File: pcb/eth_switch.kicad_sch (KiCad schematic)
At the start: 9 parts, among them IC1 IP175G, J1 100616-2

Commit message: More schematic
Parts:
- added C23: 100n, Capacitor_SMD:C_0603_1608Metric_Pad1.08x0.95mm_HandSolder, symbol Device:C
- added D3, D4, D5, D6, D7, D8: ~, LED_SMD:LED_0603_1608Metric_Pad1.05x0.95mm_HandSolder, symbol Device:LED
- added J3: Conn_01x04, Connector_PinHeader_1.00mm:PinHeader_1x04_P1.00mm_Vertical, symbol Connector_Generic:Conn_01x04
- added JP1: SolderJumper_3_Bridged12, Jumper:SolderJumper-3_P1.3mm_Bridged12_Pad1.0x1.5mm, symbol Jumper:SolderJumper_3_Bridged12
- added R19, R20: 10k, Resistor_SMD:R_0603_1608Metric_Pad0.98x0.95mm_HandSolder, symbol Device:R
- added R21, R22, R23, R24, R25, R26, R27, R28, R29, R30, R31, R32, R33, R34, R35, R36, R37, R38, R39, R40: 2R2, Resistor_SMD:R_0603_1608Metric, symbol Device:R
- added R41, R42, R43, R44, R45, R46: 330, Resistor_SMD:R_0603_1608Metric_Pad0.98x0.95mm_HandSolder, symbol Device:R
- added U5: 24LC02, Package_SO:SOIC-8_3.9x4.9mm_P1.27mm, symbol Memory_EEPROM:24LC02
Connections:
- net 1TX1_N: now reaches IC1.1 (TXOM1)
- net 1TX1_N: now also R21.2
- net 2TX2_P: now reaches IC1.10 (TXOP2)
- net 2TX2_P: now also R26.2
- net 2TX2_N: now reaches IC1.11 (TXOM2)
- net 2TX2_N: now also R25.2
- net 3RX3_P: now reaches IC1.14 (RXIP3)
- net 3RX3_P: now also R33.2
- net 3RX3_N: now reaches IC1.15 (RXIM3)
- net 3RX3_N: now also R34.2
- net 3TX3_P: now reaches IC1.16 (TXOP3)
- net 3TX3_P: now also R35.2
- net 3TX3_N: now reaches IC1.17 (TXOM3)
- net 3TX3_N: now also R36.2
- net 4TX4_N: now reaches IC1.19 (TXOM4)
- net 4TX4_N: now also R37.2
- net 1TX1_P: now reaches IC1.2 (TXOP1)
- net 1TX1_P: now also R22.2
- net 4TX4_P: now reaches IC1.20 (TXOP4)
- net 4TX4_P: now also R38.2
- net 4RX4_N: now reaches IC1.21 (RXIM4)
- net 4RX4_N: now also R39.2
- net 4RX4_P: now reaches IC1.22 (RXIP4)
- net 4RX4_P: now also R40.2
- net 1RX1_N: now reaches IC1.3 (RXIM1)
- net 1RX1_N: now also R23.2
- net PWR_OFF: now reaches IC1.31 (F_POWER_OFF_LED_/_VLAN_DIS)
- net PWR_OFF: now also R46.1
- net LINK4: now reaches IC1.32 (LINK_LED4)
- net LINK4: now also R45.1
- net LINK3: now reaches IC1.33 (LINK_LED3)
- net LINK3: now also R44.1
- net LINK2: now reaches IC1.35 (LINK_LED2/RSVD_GMAC_FILTER)
- net LINK2: now also R43.1
- net LINK1: now reaches IC1.36 (LINK_LED1/SCLK/BF_STM_DIS)
- net LINK1: now also R42.1
- net LINK0: now reaches IC1.37 (LINK_LED0/SDATA/COS_DIS)
- net LINK0: now also R41.1
- net I2C_SCL: now reaches IC1.38 (SCL/MDC)
- net I2C_SCL: now also J3.3 (Pin_3), R19.1, U5.6 (SCL)
- net I2C_SDA: now reaches IC1.39 (SDA/MDIO)
- net I2C_SDA: now also J3.2 (Pin_2), R20.1, U5.5 (SDA)
- net 1RX1_P: now reaches IC1.4 (RXIP1)
- net 1RX1_P: now also R24.2
- net 0RX0_P: now reaches IC1.44 (RXIP0)
- net 0RX0_P: now also R32.2
- net 0RX0_N: now reaches IC1.45 (RXIM0)
- net 0RX0_N: now also R31.2
- net 0TX0_P: now reaches IC1.46 (TXOP0)
- net 0TX0_P: now also R30.2
- net 0TX0_N: now reaches IC1.47 (TXOM0)
- net 0TX0_N: now also R29.2
- net 2RX2_P: now reaches IC1.8 (RXIP2)
- net 2RX2_P: now also R28.2
- net 2RX2_N: now reaches IC1.9 (RXIM2)
- net 2RX2_N: now also R27.2
- new net: D7.1 (K), R45.2
- new net: D6.1 (K), R44.2
- new net: D5.1 (K), R43.2
- new net: D4.1 (K), R42.2
- new net: D3.1 (K), R41.2
- new net: D8.1 (K), R46.2
- new net: JP1.2 (C), U5.7 (WP)
- new net +3.3V: C23.1, D3.2 (A), D4.2 (A), D5.2 (A), D6.2 (A), D7.2 (A), D8.2 (A), J3.1 (Pin_1), JP1.1 (A), R19.2, R20.2, U5.8 (VCC)
- new net GND: C23.2, J3.4 (Pin_4), JP1.3 (B), U5.1 (A0), U5.2 (A1), U5.3 (A2), U5.4 (GND)
- new net RX0_N: R31.1
- new net RX0_P: R32.1
- new net RX1_N: R23.1
- new net RX1_P: R24.1
- new net RX2_N: R27.1
- new net RX2_P: R28.1
- new net RX3_N: R34.1
- new net RX3_P: R33.1
- new net RX4_N: R39.1
- new net RX4_P: R40.1
- new net TX0_N: R29.1
- new net TX0_P: R30.1
- new net TX1_N: R21.1
- new net TX1_P: R22.1
- new net TX2_N: R25.1
- new net TX2_P: R26.1
- new net TX3_N: R36.1
- new net TX3_P: R35.1
- new net TX4_N: R37.1
- new net TX4_P: R38.1

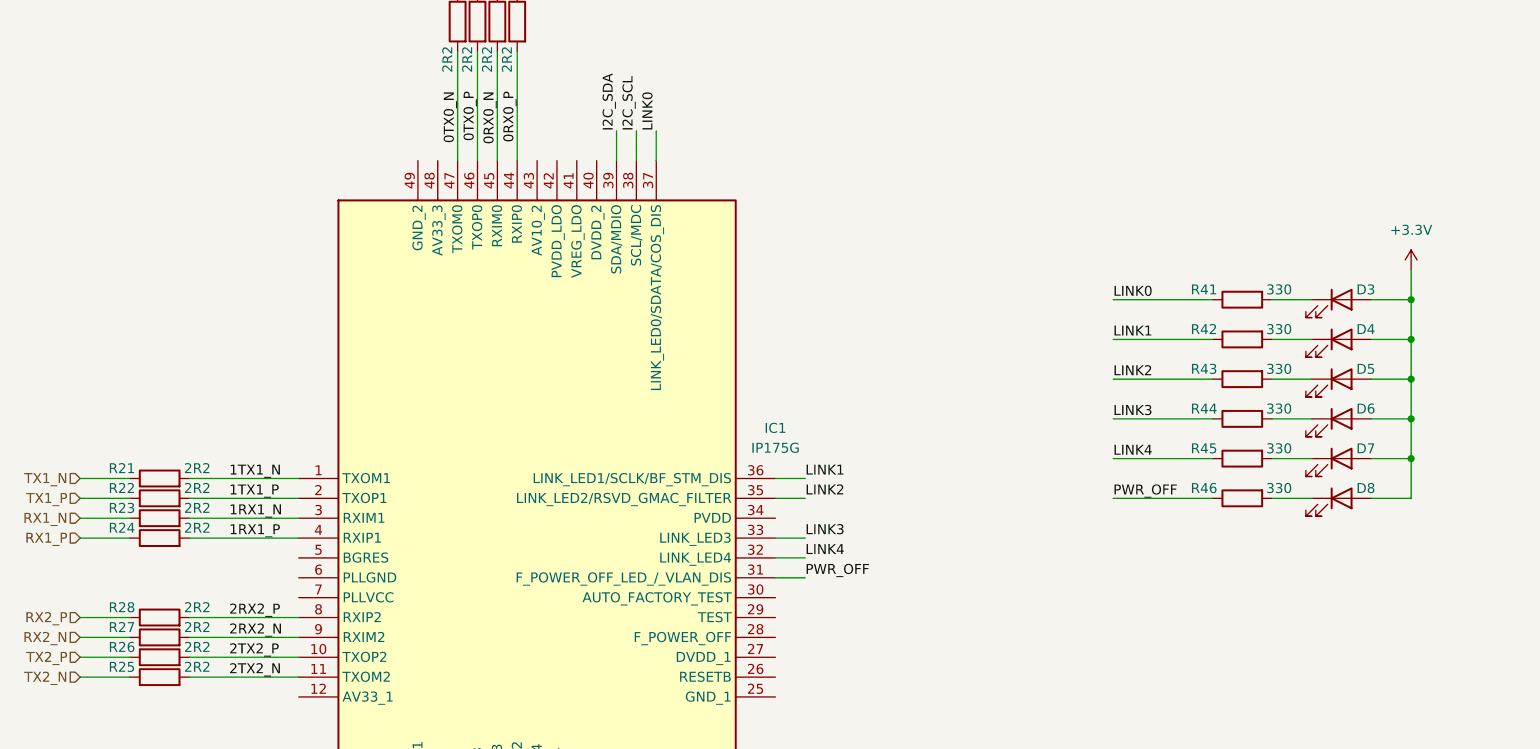
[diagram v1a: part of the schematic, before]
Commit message: Add symbols and adjust component positions in eth_switch schematic
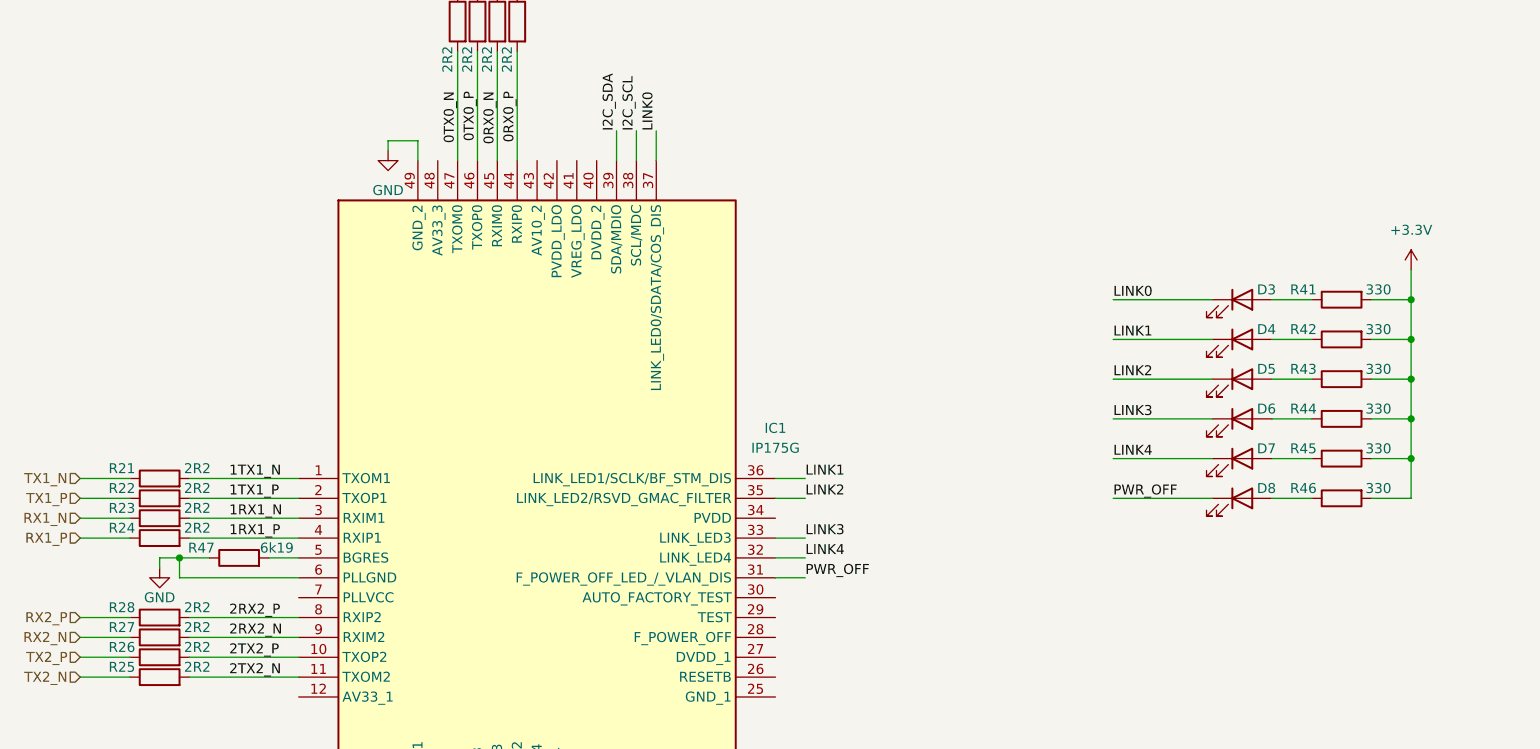
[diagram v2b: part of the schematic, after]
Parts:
- added R47: 6k19, Resistor_SMD:R_0603_1608Metric, symbol Device:R
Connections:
- net +3.3V: now also R41.2, R42.2, R43.2, R44.2, R45.2, R46.2; no longer D3.2 (A), D4.2 (A), D5.2 (A), D6.2 (A), D7.2 (A), D8.2 (A)
- net GND: now also IC1.49 (GND_2), IC1.6 (PLLGND), R47.1
- net LINK0: now also D3.1 (K); no longer R41.1
- net LINK1: now also D4.1 (K); no longer R42.1
- net LINK2: now also D5.1 (K); no longer R43.1
- net LINK3: now also D6.1 (K); no longer R44.1
- net LINK4: now also D7.1 (K); no longer R45.1
- net PWR_OFF: now also D8.1 (K); no longer R46.1
- net at IC1.5 (BGRES): now also R47.2
- new net: D7.2 (A), R45.1
- new net: D6.2 (A), R44.1
- new net: D5.2 (A), R43.1
- new net: D4.2 (A), R42.1
- new net: D3.2 (A), R41.1
- new net: D8.2 (A), R46.1
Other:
- moved on the sheet: D3, D4, D5, D6, D7, D8, R41, R42, R43, R44, R45, R46

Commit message: Sch complete, starting pcb
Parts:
- added C10, C11, C12, C13, C14, C18, C19, C22, C23, C24, C25, C26, C27, C30, C31, C32, C35, C36, C9: 100n, Capacitor_SMD:C_0603_1608Metric_Pad1.08x0.95mm_HandSolder, symbol Device:C
- added C16, C20, C28, C7: 1u, Capacitor_SMD:C_0603_1608Metric_Pad1.08x0.95mm_HandSolder, symbol Device:C
- added C17, C21, C29, C8: 10u, Capacitor_SMD:C_1206_3216Metric_Pad1.33x1.80mm_HandSolder, symbol Device:C
- added C34: 1n, Capacitor_SMD:C_0603_1608Metric_Pad1.08x0.95mm_HandSolder, symbol Device:C
- added C37, C38: 6,8n, Capacitor_SMD:C_0603_1608Metric_Pad1.08x0.95mm_HandSolder, symbol Device:C
- added C39, C40: 10n, Capacitor_SMD:C_0603_1608Metric_Pad1.08x0.95mm_HandSolder, symbol Device:C
- added C41, C42: 18p, Capacitor_SMD:C_0402_1005Metric_Pad0.74x0.62mm_HandSolder, symbol Device:C
- added C43: 1nF/2kV, Capacitor_SMD:C_1206_3216Metric_Pad1.33x1.80mm_HandSolder, symbol Device:C
- added D9: UT8413A, Package_DFN_QFN:Diodes_UDFN-10_1.0x2.5mm_P0.5mm, symbol Conn:UT8413A
- added FB1, FB2, FB3, FB4, FB5: 100 @ 100MHz, Inductor_SMD:L_0603_1608Metric_Pad1.05x0.95mm_HandSolder, symbol Device:FerriteBead_Small
- added J5: Conn_01x02, Connector_PinHeader_1.00mm:PinHeader_1x02_P1.00mm_Vertical, symbol Connector_Generic:Conn_01x02
- added JP3, JP5: SolderJumper_2_Open, Jumper:SolderJumper-2_P1.3mm_Open_RoundedPad1.0x1.5mm, symbol Jumper:SolderJumper_2_Open
- added JP4: SolderJumper_2_Bridged, Jumper:SolderJumper-2_P1.3mm_Bridged_RoundedPad1.0x1.5mm, symbol Jumper:SolderJumper_2_Bridged
- added R34, R35, R36: 10k, Resistor_SMD:R_0603_1608Metric_Pad0.98x0.95mm_HandSolder, symbol Device:R
- added R41, R42: 49R9, Resistor_SMD:R_0603_1608Metric_Pad0.98x0.95mm_HandSolder, symbol Device:R
- added R43: 10R, Resistor_SMD:R_0603_1608Metric_Pad0.98x0.95mm_HandSolder, symbol Device:R
- added R44: 1M, Resistor_SMD:R_0603_1608Metric, symbol Device:R
- added R45, R46: 82R, Resistor_SMD:R_0603_1608Metric_Pad0.98x0.95mm_HandSolder, symbol Device:R
- added R55, R56: 75R, Resistor_SMD:R_0603_1608Metric_Pad0.98x0.95mm_HandSolder, symbol Device:R
- added R57, R58: 150R, Resistor_SMD:R_0603_1608Metric_Pad0.98x0.95mm_HandSolder, symbol Device:R
- added T1: H1102NL, SamacSys_Parts:SOIC127P940X597-16N, symbol SamacSys_Parts:H1102NL
- added U4, U5: USBLC6-2SC6, Package_TO_SOT_SMD:SOT-23-6_Handsoldering, symbol Power_Protection:USBLC6-2SC6
- added Y2: 3225-25M-SR, Crystal:Crystal_SMD_3225-4Pin_3.2x2.5mm, symbol Device:Crystal_GND24
- renumbered C1 to C15, C23 to C33, J1 to J3, J3 to J4, JP1 to JP2, R1 to R11, R2 to R12, R3 to R13, R4 to R14, R5 to R15, R6 to R16, R29 to R17, R30 to R18, R31 to R19, R32 to R20, R41 to R21, R19 to R22, R20 to R23, R42 to R24, R43 to R25, R44 to R26, R45 to R27, R21 to R28, R22 to R29, R46 to R30, R23 to R31, R24 to R32, R47 to R33, R28 to R37, R27 to R38, R26 to R39, R25 to R40, R33 to R47, R34 to R48, R35 to R49, R36 to R50, R37 to R51, R38 to R52, R39 to R53, R40 to R54, U5 to U3
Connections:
- net +3.3V: now also C16.1, C17.1, C18.1, C19.1, FB3.1, FB4.1, FB5.1
- net Earth: now also C43.2
- net GND: now also IC1.25 (GND_1), C10.2, C11.2, C12.2, C13.2, C14.2, C16.2, C17.2, C18.2, C19.2, C20.2, C21.2, C22.2, C23.2, C24.2, C25.2, C26.2, C27.2, C28.2, C29.2, C30.2, C31.2, C32.2, C34.1, C35.2, C36.2, C39.1, C40.2, C41.2, C42.2, C7.2, C8.2, C9.2, D9.3, D9.8, J5.2 (Pin_2), JP4.2 (B), JP5.1 (A), U4.2 (GND), U5.2 (GND), Y2.2, Y2.4
- net RX+: now also R57.1, T1.11 (RX+)
- net RX-: now also R58.1, T1.9 (RX-)
- net RX4_N: now also D9.1, D9.10, U5.3 (I/O2)
- net RX4_P: now also D9.2, D9.9, U5.1 (I/O1)
- net TX+: now also T1.16 (TX+)
- net TX-: now also T1.14 (TX-)
- net TX4_N: now also D9.4, D9.7, U4.3 (I/O2)
- net TX4_P: now also D9.5, D9.6, U4.1 (I/O1)
- net REG_IN: now reaches IC1.12 (AV33_1)
- net REG_IN: now also IC1.18 (AV33_2), IC1.42 (PVDD_LDO), IC1.48 (AV33_3), IC1.7 (PLLVCC), C20.1, C21.1, C22.1, C23.1, C24.1, C25.1, C26.1, C27.1, FB3.2
- net VDD10: now reaches IC1.13 (AV10_1)
- net VDD10: now also IC1.43 (AV10_2), C11.1, C12.1, FB1.2
- net at IC1.23 (OSCI): now also C41.1, R44.1, Y2.1
- net at IC1.24 (X2): now also C42.1, R44.2, Y2.3
- net at IC1.26 (RESETB): now also C34.2, J5.1 (Pin_1), R36.1
- net DVDD: now reaches IC1.27 (DVDD_1)
- net DVDD: now also IC1.40 (DVDD_2), C13.1, C14.1, FB2.2
- net at IC1.28 (F_POWER_OFF): now also JP5.2 (B), R35.1
- net at IC1.29 (TEST): now also JP4.1 (A)
- net at IC1.30 (AUTO_FACTORY_TEST): now also JP3.1 (A)
- net DVCC: now reaches IC1.34 (PVDD)
- net DVCC: now also C30.1, C31.1, C32.1, FB4.2, R34.2, R35.2, R36.2
- net REG_OUT: now reaches IC1.41 (VREG_LDO)
- net REG_OUT: now also C10.1, C7.1, C8.1, C9.1, FB1.1, FB2.1
- new net: C43.1, R55.2, R56.2, R57.2, R58.2
- new net: JP3.2 (B), R34.1
- new net: C35.1, C36.1, FB5.2, R41.1, R42.1, R43.1, U4.5 (VBUS), U5.5 (VBUS)
- new net: R55.1, T1.10 (NC_3)
- new net: C39.2, R43.2, T1.2 (CT_1)
- new net: C40.1, R45.2, R46.2, T1.7 (CT_2)
- new net: R56.1, T1.15 (NC_6)
- new net: C37.1, T1.6 (RD+)
- new net: C38.1, T1.8 (RD-)
- new net RD+: C37.2, R45.1, U5.6 (I/O1)
- new net RD-: C38.2, R46.1, U5.4 (I/O2)
- new net TD+: R42.2, T1.1 (TD+), U4.6 (I/O1)
- new net TD-: R41.2, T1.3 (TD-), U4.4 (I/O2)
- no-connect marks 0 -> 4
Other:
- moved on the sheet: C15, J3, R11, R12, R13, R14, R15, R16, R28, R29, R31, R32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

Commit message: Routing
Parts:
- removed D9: UT8413A, Package_DFN_QFN:Diodes_UDFN-10_1.0x2.5mm_P0.5mm, symbol Conn:UT8413A
- C41, C42, Y2: now fitted
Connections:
- net DVCC: now also C28.1, C29.1
- net RD+: now also U5.1 (I/O1); no longer U5.6 (I/O1)
- net RD-: now also U5.3 (I/O2); no longer U5.4 (I/O2)
- net RX4_N: now also U5.4 (I/O2); no longer U5.3 (I/O2)
- net RX4_P: now also U5.6 (I/O1); no longer U5.1 (I/O1)
- net TD+: now also U4.1 (I/O1); no longer U4.6 (I/O1)
- net TD-: now also U4.3 (I/O2); no longer U4.4 (I/O2)
- net TX4_N: now also U4.4 (I/O2); no longer U4.3 (I/O2)
- net TX4_P: now also U4.6 (I/O1); no longer U4.1 (I/O1)
